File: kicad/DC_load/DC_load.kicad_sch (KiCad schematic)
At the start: 4 parts

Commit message: All cool
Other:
- sheet Microcontroller ports: added SINK_TEMP; removed none
- sheet Power_stage ports: added SINK_TEMP; removed none
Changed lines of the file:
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@@
+	(wire
+		(pts
+			(xy 124.46 107.95) (xy 134.62 107.95)
+		)
+		(stroke
+			(width 0)
+			(type default)
+		)
+	)
 	(wire
 		(pts
@@
 			)
 		)
+		(pin "SINK_TEMP" input
+			(at 124.46 107.95 0)
+			(effects
+				(font
+					(size 1.27 1.27)
+				)
+				(justify right)
+			)
+		)
 		(instances
 			(project "DC_load"
@@
 			(effects
 				(font
+					(size 1.27 1.27)
+				)
+				(justify left)
+			)
+		)
+		(pin "SINK_TEMP" output
+			(at 134.62 107.95 180)
+			(effects
+				(font

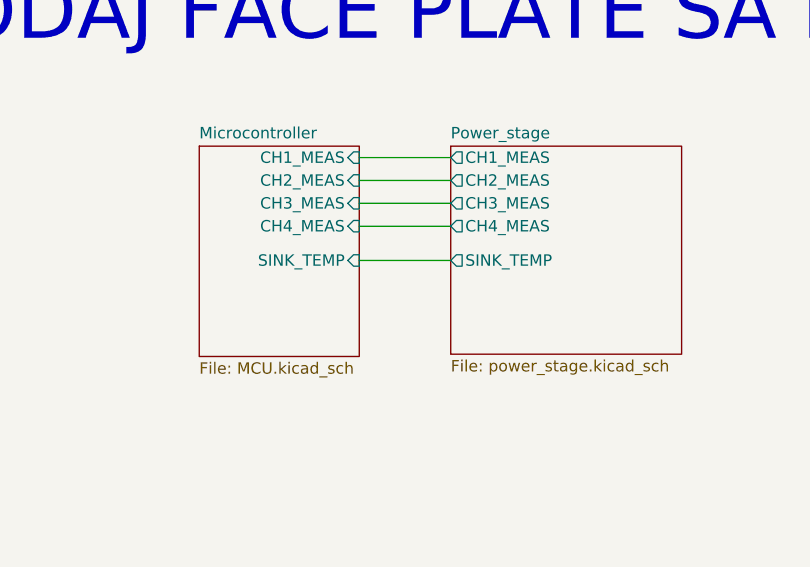
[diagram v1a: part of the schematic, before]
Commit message: Added voltage sense
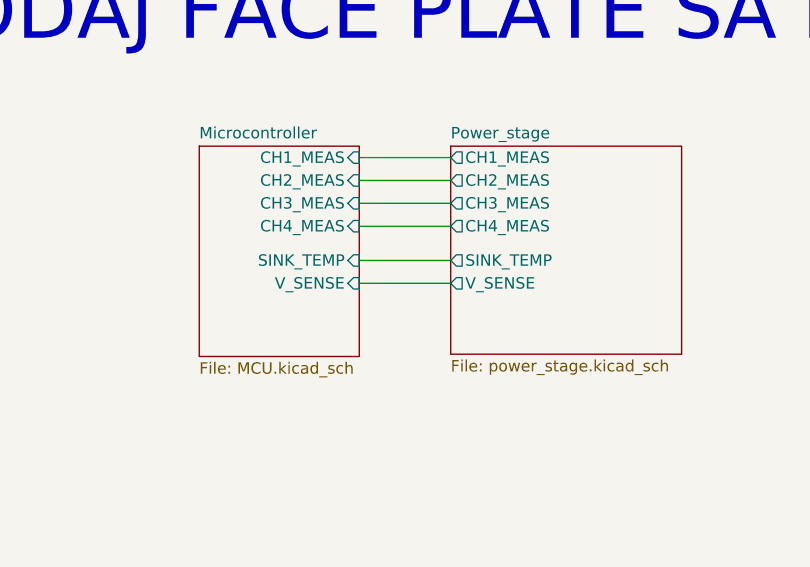
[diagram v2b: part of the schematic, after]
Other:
- sheet Microcontroller ports: added V_SENSE; removed none
- sheet Power_stage ports: added V_SENSE; removed none
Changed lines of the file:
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@@
+	(wire
+		(pts
+			(xy 124.46 110.49) (xy 134.62 110.49)
+		)
+		(stroke
+			(width 0)
+			(type default)
+		)
+	)
 	(wire
 		(pts
@@
 			)
 		)
+		(pin "V_SENSE" input
+			(at 124.46 110.49 0)
+			(effects
+				(font
+					(size 1.27 1.27)
+				)
+				(justify right)
+			)
+		)
 		(instances
 			(project "DC_load"
@@
 			(effects
 				(font
+					(size 1.27 1.27)
+				)
+				(justify left)
+			)
+		)
+		(pin "V_SENSE" output
+			(at 134.62 110.49 180)
+			(effects
+				(font

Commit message: note.
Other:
- note added: "3D print face plate je bolja ideja"
- note removed: "DODAJ FACE PLATE SA KUKAMA ZA SENSE"
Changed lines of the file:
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@@
 	(generator_version "9.0")
 	(paper "A4")
-	(text "DODAJ FACE PLATE SA KUKAMA ZA SENSE"
+	(text "3D print face plate je bolja ideja\n"
 		(exclude_from_sim no)
 		(at 164.846 80.518 0)

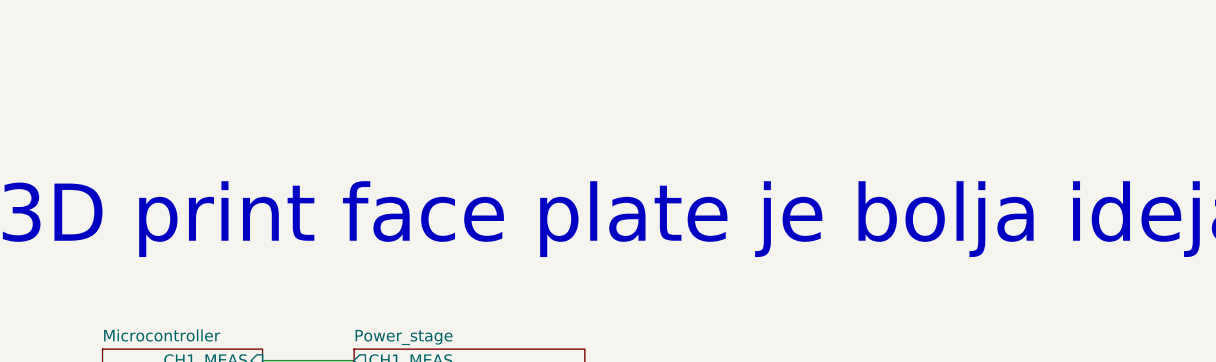
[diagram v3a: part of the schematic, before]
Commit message: DC fan boost converter added.
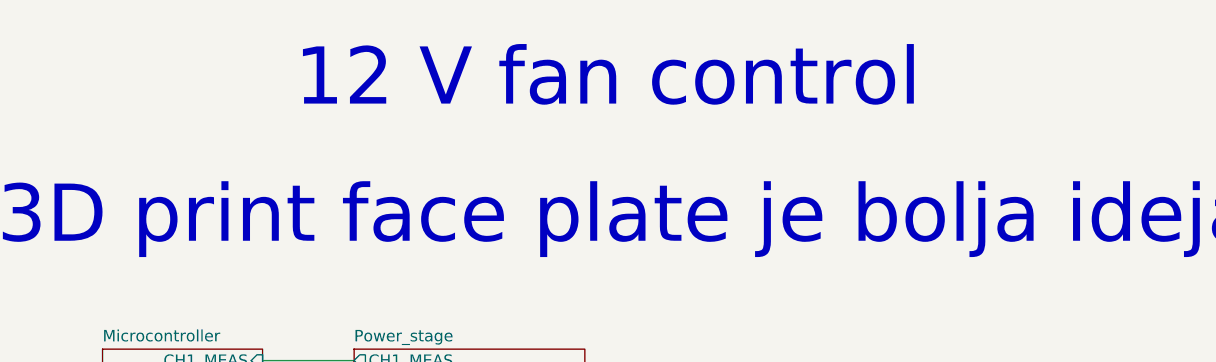
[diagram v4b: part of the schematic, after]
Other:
- note added: "12 V fan control"
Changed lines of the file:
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@@
+		)
+	)
+	(text "12 V fan control\n"
+		(exclude_from_sim no)
+		(at 162.814 65.278 0)
+		(effects
+			(font
+				(size 6.35 6.35)
+			)
 		)
 	)

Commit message: Done???.
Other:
- note removed: "12 V fan control"
- note removed: "3D print face plate je bolja ideja"
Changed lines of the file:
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@@
 	(generator_version "9.0")
 	(paper "A4")
-	(text "3D print face plate je bolja ideja\n"
-		(exclude_from_sim no)
-		(at 164.846 80.518 0)
-		(effects
-			(font
-				(size 6.35 6.35)
-			)
-		)
-	)
-	(text "12 V fan control\n"
-		(exclude_from_sim no)
-		(at 162.814 65.278 0)
-		(effects
-			(font
-				(size 6.35 6.35)
-			)
-		)
-	)
 	(wire
 		(pts

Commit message: Ready for production.
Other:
- title: (none) -> DC load
- moved on the sheet: H1, H2, H3, H4
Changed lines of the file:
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@@
 	(generator "eeschema")
 	(generator_version "9.0")
-	(paper "A4")
-	(wire
-		(pts
-			(xy 124.46 110.49) (xy 134.62 110.49)
-		)
-		(stroke
-			(width 0)
-			(type default)
-		)
-	)
-	(wire
-		(pts
-			(xy 124.46 99.06) (xy 134.62 99.06)
-		)
-		(stroke
-			(width 0)
-			(type default)
-		)
-	)
-	(wire
-		(pts
-			(xy 124.46 101.6) (xy 134.62 101.6)
-		)
-		(stroke
-			(width 0)
-			(type default)
-		)
-	)
-	(wire
-		(pts
-			(xy 124.46 107.95) (xy 134.62 107.95)
-		)
-		(stroke
-			(width 0)
-			(type default)
-		)
-	)
-	(wire
-		(pts
-			(xy 124.46 104.14) (xy 134.62 104.14)
-		)
-		(stroke
-			(width 0)
-			(type default)
-		)
-	)
-	(wire
-		(pts
-			(xy 124.46 96.52) (xy 134.62 96.52)
+	(paper "A5")
+	(title_block
+		(title "DC load")
+	)
+	(wire
+		(pts
+			(xy 104.14 58.42) (xy 114.3 58.42)
+		)
+		(stroke
+			(width 0)
+			(type default)
+		)
+	)
+	(wire
+		(pts
+			(xy 104.14 46.99) (xy 114.3 46.99)
+		)
+		(stroke
+			(width 0)
+			(type default)
+		)
+	)
+	(wire
+		(pts
+			(xy 104.14 49.53) (xy 114.3 49.53)
+		)
+		(stroke
+			(width 0)
+			(type default)
+		)
+	)
+	(wire
+		(pts
+			(xy 104.14 55.88) (xy 114.3 55.88)
+		)
+		(stroke
+			(width 0)
+			(type default)
+		)
+	)
+	(wire
+		(pts
+			(xy 104.14 52.07) (xy 114.3 52.07)
+		)
+		(stroke
+			(width 0)
+			(type default)
+		)
+	)
+	(wire
+		(pts
+			(xy 104.14 44.45) (xy 114.3 44.45)
 		)
 		(stroke
@@
 	(symbol
 		(lib_id "Mechanical:MountingHole")
-		(at 43.18 186.69 0)
+		(at 30.48 121.92 0)
 		(unit 1)
 		(exclude_from_sim no)
@@
 		(fields_autoplaced yes)
 		(property "Reference" "H1"
-			(at 45.72 185.4199 0)
+			(at 33.02 120.6499 0)
 			(effects
 				(font
@@
 		)
 		(property "Value" "MountingHole"
-			(at 45.72 187.9599 0)
+			(at 33.02 123.1899 0)
 			(effects
 				(font
@@
 		)
 		(property "Footprint" "DC_load:M3_hole_with_spacer"
-			(at 43.18 186.69 0)
+			(at 30.48 121.92 0)
 			(effects
 				(font
@@
 		)
 		(property "Datasheet" "~"
-			(at 43.18 186.69 0)
+			(at 30.48 121.92 0)
 			(effects
 				(font
@@
 		)
 		(property "Description" "Mounting Hole without connection"
-			(at 43.18 186.69 0)
+			(at 30.48 121.92 0)
 			(effects
 				(font
@@
 	(symbol
 		(lib_id "Mechanical:MountingHole")
-		(at 64.77 186.69 0)
+		(at 52.07 121.92 0)
 		(unit 1)
 		(exclude_from_sim no)
@@
 		(fields_autoplaced yes)
 		(property "Reference" "H2"
-			(at 67.31 185.4199 0)
+			(at 54.61 120.6499 0)
 			(effects
 				(font
@@
 		)
 		(property "Value" "MountingHole"
-			(at 67.31 187.9599 0)
+			(at 54.61 123.1899 0)
 			(effects
 				(font
@@
 		)
 		(property "Footprint" "DC_load:M3_hole_with_spacer"
-			(at 64.77 186.69 0)
+			(at 52.07 121.92 0)
 			(effects
 				(font
@@
 		)
 		(property "Datasheet" "~"
-			(at 64.77 186.69 0)
+			(at 52.07 121.92 0)
 			(effects
 				(font
@@
 		)
 		(property "Description" "Mounting Hole without connection"
-			(at 64.77 186.69 0)
+			(at 52.07 121.92 0)
 			(effects
 				(font
@@
 	(symbol
 		(lib_id "Mechanical:MountingHole")
-		(at 43.18 193.04 0)
+		(at 30.48 128.27 0)
 		(unit 1)
 		(exclude_from_sim no)
@@
 		(fields_autoplaced yes)
 		(property "Reference" "H3"
-			(at 45.72 191.7699 0)
+			(at 33.02 126.9999 0)
 			(effects
 				(font
@@
 		)
 		(property "Value" "MountingHole"
-			(at 45.72 194.3099 0)
+			(at 33.02 129.5399 0)
 			(effects
 				(font
@@
 		)
 		(property "Footprint" "DC_load:M3_hole_with_spacer"
-			(at 43.18 193.04 0)
+			(at 30.48 128.27 0)
 			(effects
 				(font
@@
 		)
 		(property "Datasheet" "~"
-			(at 43.18 193.04 0)
+			(at 30.48 128.27 0)
 			(effects
 				(font
@@
 		)
 		(property "Description" "Mounting Hole without connection"
-			(at 43.18 193.04 0)
+			(at 30.48 128.27 0)
 			(effects
 				(font
@@
 	(symbol
 		(lib_id "Mechanical:MountingHole")
-		(at 64.77 193.04 0)
+		(at 52.07 128.27 0)
 		(unit 1)
 		(exclude_from_sim no)
@@
 		(fields_autoplaced yes)
 		(property "Reference" "H4"
-			(at 67.31 191.7699 0)
+			(at 54.61 126.9999 0)
 			(effects
 				(font
@@
 		)
 		(property "Value" "MountingHole"
-			(at 67.31 194.3099 0)
+			(at 54.61 129.5399 0)
 			(effects
 				(font
@@
 		)
 		(property "Footprint" "DC_load:M3_hole_with_spacer"
-			(at 64.77 193.04 0)
+			(at 52.07 128.27 0)
 			(effects
 				(font
@@
 		)
 		(property "Datasheet" "~"
-			(at 64.77 193.04 0)
+			(at 52.07 128.27 0)
 			(effects
 				(font
@@
 		)
 		(property "Description" "Mounting Hole without connection"
-			(at 64.77 193.04 0)
+			(at 52.07 128.27 0)
 			(effects
 				(font
@@
 	)
 	(sheet
-		(at 106.68 95.25)
+		(at 86.36 43.18)
 		(size 17.78 23.368)
 		(exclude_from_sim no)
@@
 		)
 		(property "Sheetname" "Microcontroller"
-			(at 106.68 94.5384 0)
+			(at 86.36 42.4684 0)
 			(effects
 				(font
@@
 		)
 		(property "Sheetfile" "MCU.kicad_sch"
-			(at 106.68 119.2026 0)
+			(at 86.36 67.1326 0)
 			(effects
 				(font
@@
 		)
 		(pin "CH1_MEAS" input
-			(at 124.46 96.52 0)
+			(at 104.14 44.45 0)
 			(effects
 				(font
@@
 		)
 		(pin "CH4_MEAS" input
-			(at 124.46 104.14 0)
+			(at 104.14 52.07 0)
 			(effects
 				(font
@@
 		)
 		(pin "CH2_MEAS" input
-			(at 124.46 99.06 0)
+			(at 104.14 46.99 0)
 			(effects
 				(font
@@
 		)
 		(pin "CH3_MEAS" input
-			(at 124.46 101.6 0)
+			(at 104.14 49.53 0)
 			(effects
 				(font
@@
 		)
 		(pin "SINK_TEMP" input
-			(at 124.46 107.95 0)
+			(at 104.14 55.88 0)
 			(effects
 				(font
@@
 		)
 		(pin "V_SENSE" input
-			(at 124.46 110.49 0)
+			(at 104.14 58.42 0)
 			(effects
 				(font
@@
 	)
 	(sheet
-		(at 134.62 95.25)
-		(size 25.654 23.114)
+		(at 114.3 43.18)
+		(size 17.78 23.114)
 		(exclude_from_sim no)
 		(in_bom yes)
@@
 		)
 		(property "Sheetname" "Power_stage"
-			(at 134.62 94.5384 0)
+			(at 114.3 42.4684 0)
 			(effects
 				(font
@@
 		)
 		(property "Sheetfile" "power_stage.kicad_sch"
-			(at 134.62 118.9486 0)
+			(at 114.3 66.8786 0)
 			(effects
 				(font
@@
 		)
 		(pin "CH4_MEAS" output
-			(at 134.62 104.14 180)
+			(at 114.3 52.07 180)
 			(effects
 				(font
@@
 		)
 		(pin "CH1_MEAS" output
-			(at 134.62 96.52 180)
+			(at 114.3 44.45 180)
 			(effects
 				(font
@@
 		)
 		(pin "CH3_MEAS" output
-			(at 134.62 101.6 180)
+			(at 114.3 49.53 180)
 			(effects
 				(font
@@
 		)
 		(pin "CH2_MEAS" output
-			(at 134.62 99.06 180)
+			(at 114.3 46.99 180)
 			(effects
 				(font
@@
 		)
 		(pin "SINK_TEMP" output
-			(at 134.62 107.95 180)
+			(at 114.3 55.88 180)
 			(effects
 				(font
@@
 		)
 		(pin "V_SENSE" output
-			(at 134.62 110.49 180)
-			(effects
-				(font
+			(at 114.3 58.42 180)
+			(effects
+				(font

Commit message: Sim, comp, power.
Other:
- note added: "JLC ima tastere"
- note added: "dodaj par LEDova"
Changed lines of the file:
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@@
 		(title "DC load")
+	)
+	(text "dodaj par LEDova\n"
+		(exclude_from_sim no)
+		(at 103.124 79.502 0)
+		(effects
+			(font
+				(size 4 4)
+			)
+		)
+	)
+	(text "JLC ima tastere "
+		(exclude_from_sim no)
+		(at 101.346 87.376 0)
+		(effects
+			(font
+				(size 4 4)
+			)
+		)
 	)
 	(wire

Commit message: Schem Schem.
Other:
- note removed: "JLC ima tastere"
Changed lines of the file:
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@@
-		)
-	)
-	(text "JLC ima tastere "
-		(exclude_from_sim no)
-		(at 101.346 87.376 0)
-		(effects
-			(font
-				(size 4 4)
-			)
 		)
 	)
